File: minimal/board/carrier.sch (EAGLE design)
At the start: 28 parts, among them U1 LPC810M021FN8FP-DIL08, U2 LPC810M021FN8FP-DIL08, U3 LPC810M021FN8FP-DIL08

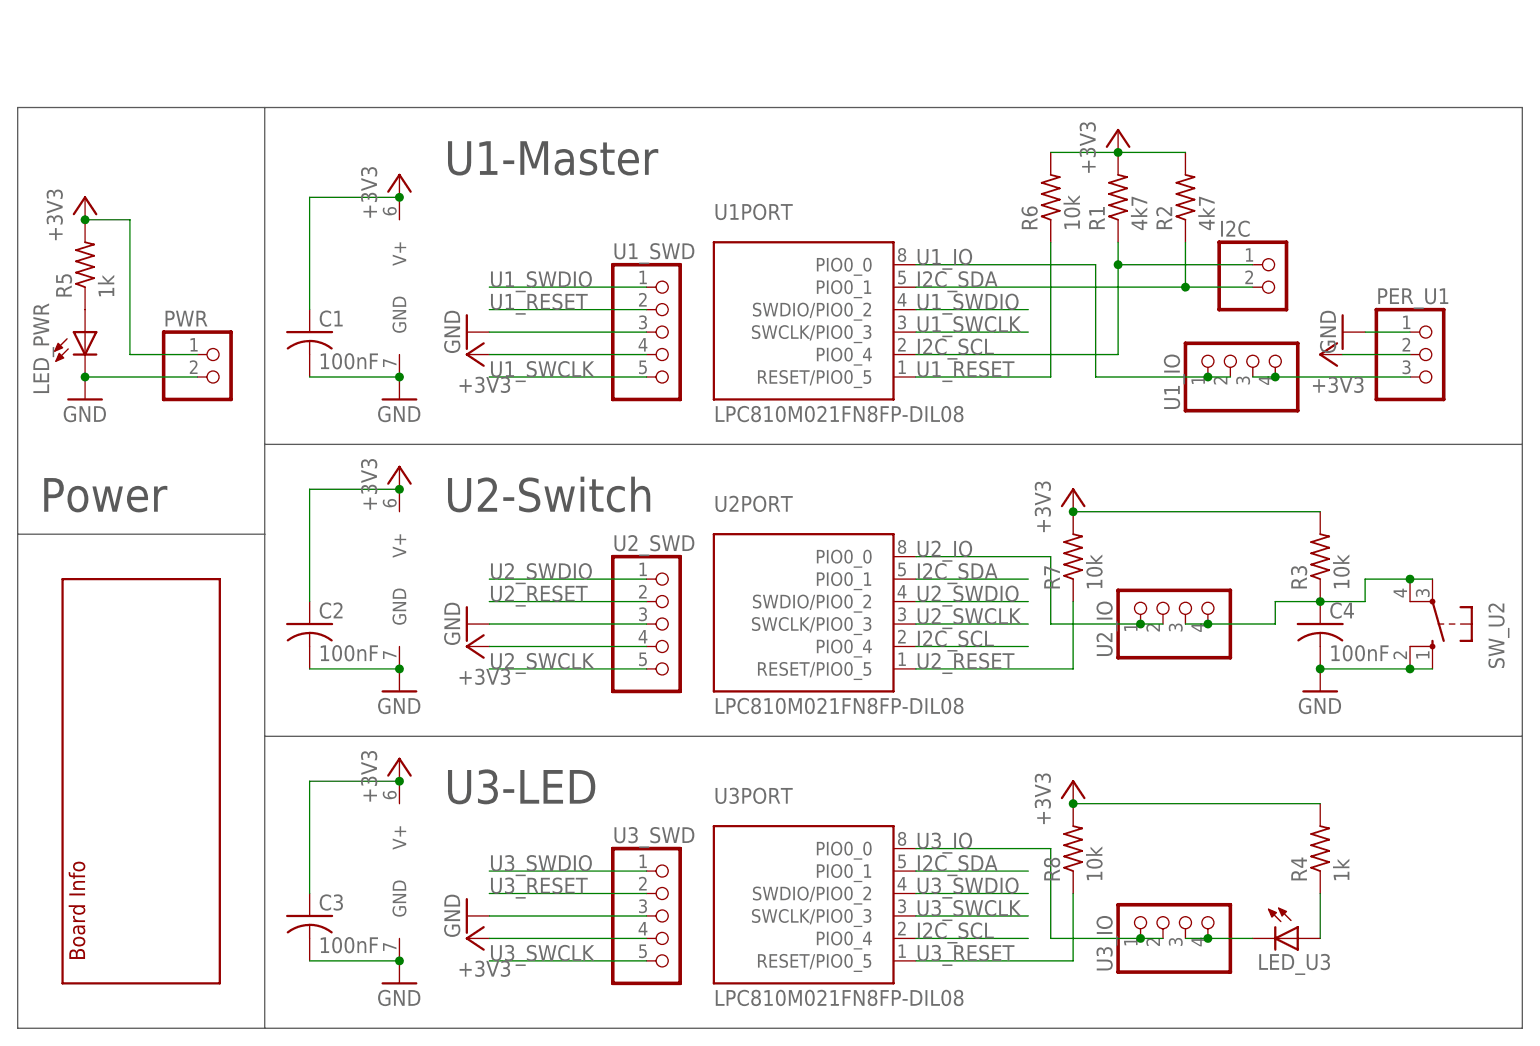
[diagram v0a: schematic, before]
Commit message: Adding all boards for minimal and carrier board with MKL05Z32
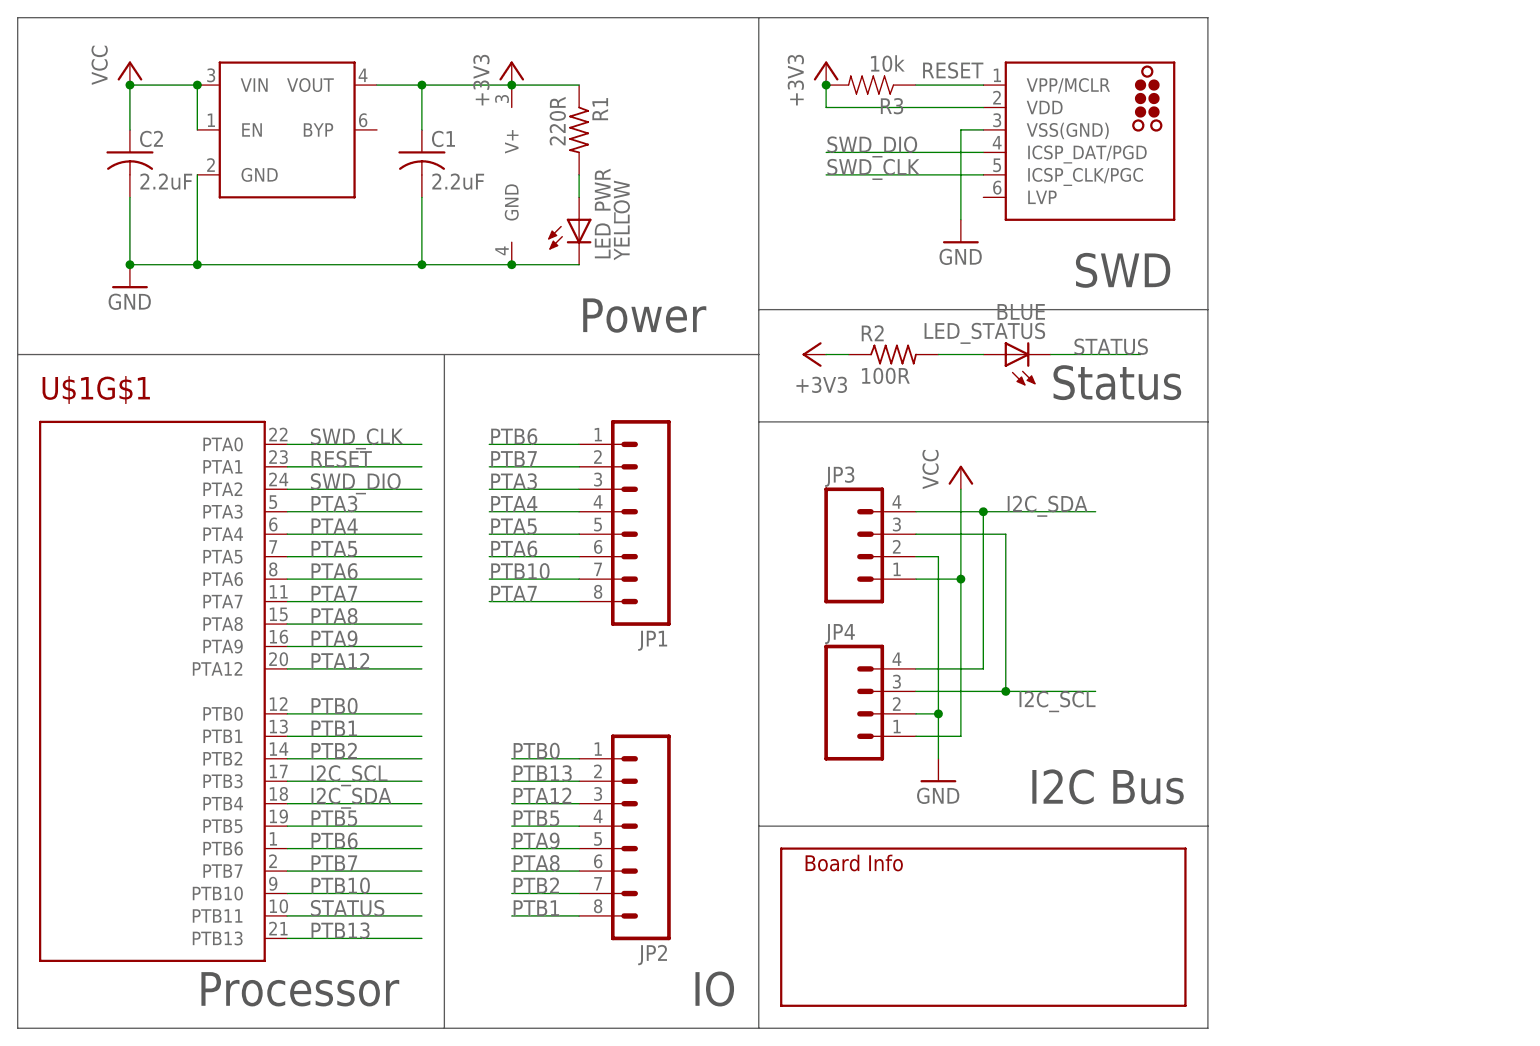
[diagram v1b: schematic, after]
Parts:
- removed C3, C4: 100nF, rcl:C-US025-025X050
- removed I2C, PWR: (no value), pinhead:PINHD-1X2
- removed LED_U3: (no value), led:LED5MM
- removed PER_U1: (no value), pinhead:PINHD-1X3
- removed R4, R5: 1k, rcl:R-US_0204/2V
- removed R6, R7, R8: 10k, rcl:R-US_0204/7
- removed SW_U2: (no value), switch-omron:10-XX
- removed U1, U2, U3: LPC810M021FN8FP-DIL08, modular_robotics:LPC810M021FN8FP-DIL08
- removed U1_IO, U2_IO, U3_IO: (no value), pinhead:PINHD-1X4
- removed U1_SWD, U2_SWD, U3_SWD: (no value), pinhead:PINHD-1X5
- added J1: (no value), tag-connect:TC2030-MCP-NL
- added JP1, JP2: (no value), SparkFun-Connectors:M081X08
- added JP3, JP4: (no value), SparkFun-Connectors:M04PTH
- added LED_STATUS: BLUE, led:LEDSML0603
- added U$2: MIC5305-MLF, modular_robotics:MIC5305-MLF
- added U$3: INFO, modular_robotics:INFO
- C1, C2: value 100nF -> 2.2uF; device rcl:C-US025-025X050 -> rcl:C-USC0402
- LED_PWR: value (none) -> YELLOW; device led:LED5MM -> led:LEDSML0603
- R1: value 4k7 -> 220R; device rcl:R-US_0204/7 -> rcl:R-US_R0402
- R2: value 4k7 -> 100R; device rcl:R-US_0204/7 -> rcl:R-US_R0402
- R3: device rcl:R-US_0204/2V -> biomimetic:RESISTOR0402-RES
- U$1: value INFO -> MKL05Z32VFK4-QFN; device modular_robotics:INFO -> modular_robotics:MKL05Z32VFK4-QFN; AUTHOR Austin Buchan -> (none); DATE May 29, 2015 -> (none); DESIGN MinimalModRob -> (none); ORGANIZATION UC Berkeley ASPIRE -> (none); REVISION r0.0 -> (none)
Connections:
- removed net N$3: PER_U1.3, U1_IO.3, U1_IO.4
- removed net N$4: LED_U3.A, R4.1
- removed net N$5: LED_U3.C, U3_IO.3, U3_IO.4
- removed net U1_IO: U1PORT.PIO0_0, U1_IO.1, U1_IO.2
- removed net U1_RESET: R6.1, U1PORT.RESET/PIO0_5, U1_SWD.2
- removed net U1_SWCLK: U1PORT.SWCLK/PIO0_3, U1_SWD.5
- removed net U1_SWDIO: U1PORT.SWDIO/PIO0_2, U1_SWD.1
- removed net U2_IO: U2PORT.PIO0_0, U2_IO.1, U2_IO.2
- removed net U2_RESET: R7.1, U2PORT.RESET/PIO0_5, U2_SWD.2
- removed net U2_SWCLK: U2PORT.SWCLK/PIO0_3, U2_SWD.5
- removed net U2_SWDIO: U2PORT.SWDIO/PIO0_2, U2_SWD.1
- removed net U3_IO: U3PORT.PIO0_0, U3_IO.1, U3_IO.2
- removed net U3_RESET: R8.1, U3PORT.RESET/PIO0_5, U3_SWD.2
- removed net U3_SWCLK: U3PORT.SWCLK/PIO0_3, U3_SWD.5
- removed net U3_SWDIO: U3PORT.SWDIO/PIO0_2, U3_SWD.1
- new net PTA12: JP2.3, U$1G$1.PTA12
- new net PTA3: JP1.3, U$1G$1.PTA3
- new net PTA4: JP1.4, U$1G$1.PTA4
- new net PTA5: JP1.5, U$1G$1.PTA5
- new net PTA6: JP1.6, U$1G$1.PTA6
- new net PTA7: JP1.8, U$1G$1.PTA7
- new net PTA8: JP2.6, U$1G$1.PTA8
- new net PTA9: JP2.5, U$1G$1.PTA9
- new net PTB0: JP2.1, U$1G$1.PTB0
- new net PTB1: JP2.8, U$1G$1.PTB1
- new net PTB10: JP1.7, U$1G$1.PTB10
- new net PTB13: JP2.2, U$1G$1.PTB13
- new net PTB2: JP2.7, U$1G$1.PTB2
- new net PTB5: JP2.4, U$1G$1.PTB5
- new net PTB6: JP1.1, U$1G$1.PTB6
- new net PTB7: JP1.2, U$1G$1.PTB7
- new net RESET: J1.VPP/MCLR, R3.1, U$1G$1.PTA1
- new net STATUS: LED_STATUS.C, U$1G$1.PTB11
- new net SWD_CLK: J1.ICSP_CLK/PGC, U$1G$1.PTA0
- new net SWD_DIO: J1.ICSP_DAT/PGD, U$1G$1.PTA2
- new net VCC: C2.1, JP3.1, JP4.1, U$2.EN, U$2.VIN
- net +3V3: now also J1.VDD, R1.1, R2.1, U$1G$2.V+, U$2.VOUT; no longer C2.1, C3.1, PER_U1.2, PWR.1, R1.2, R2.2, R4.2, R5.2, R6.2, R7.2, R8.2, U1PWR.V+, U1_SWD.4, U2PWR.V+, U2_SWD.4, U3PWR.V+, U3_SWD.4
- net GND: now also J1.VSS(GND), JP3.2, JP4.2, U$1G$2.GND, U$2.GND; no longer C3.2, C4.2, PER_U1.1, PWR.2, SW_U2.S, SW_U2.S1, U1PWR.GND, U1_SWD.3, U2PWR.GND, U2_SWD.3, U3PWR.GND, U3_SWD.3
- net I2C_SCL: now also JP3.3, JP4.3, U$1G$1.PTB3; no longer I2C.1, R1.1, U1PORT.PIO0_4, U2PORT.PIO0_4, U3PORT.PIO0_4
- net I2C_SDA: now also JP3.4, JP4.4, U$1G$1.PTB4; no longer I2C.2, R2.1, U1PORT.PIO0_1, U2PORT.PIO0_1, U3PORT.PIO0_1
- net N$1: now also R1.2; no longer R5.1
- net N$2: now also LED_STATUS.A, R2.2; no longer C4.1, R3.1, SW_U2.P, SW_U2.P1, U2_IO.3, U2_IO.4
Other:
- note added: "I2C Bus"
- note added: "IO"
- note added: "Processor"
- note added: "SWD"
- note added: "Status"
- note removed: "U1-Master"
- note removed: "U2-Switch"
- note removed: "U3-LED"
- moved on the sheet: C1, C2, LED_PWR, R1, R2, R3
